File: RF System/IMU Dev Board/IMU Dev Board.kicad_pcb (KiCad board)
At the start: 2 copper layers, 27 x 26.5 mm, 12 parts, among them J1 Conn_01x08_Pin, J2 Conn_01x08_Pin, U1 BMI088

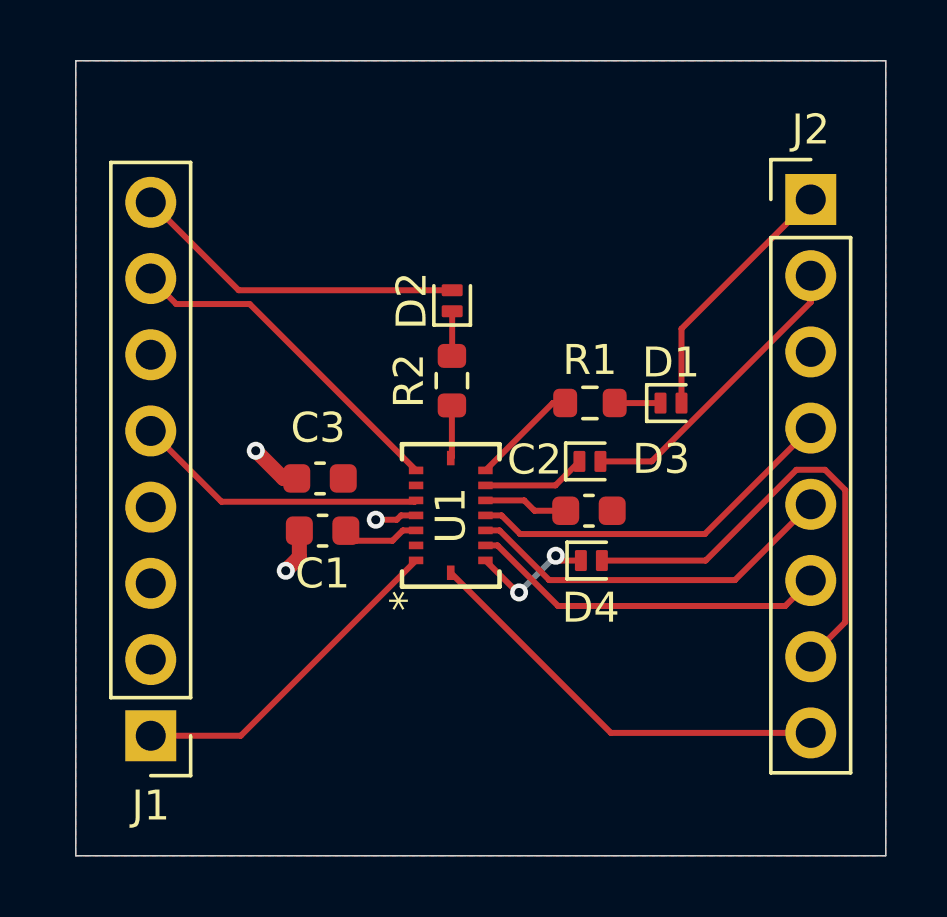
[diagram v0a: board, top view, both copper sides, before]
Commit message: IMU Dev Done
Finished IMU dev board and cleared all ERC and DRC. Design is controlled by the technical datasheet which required a strict symmetrical design within a few mm of each side of the IMU.
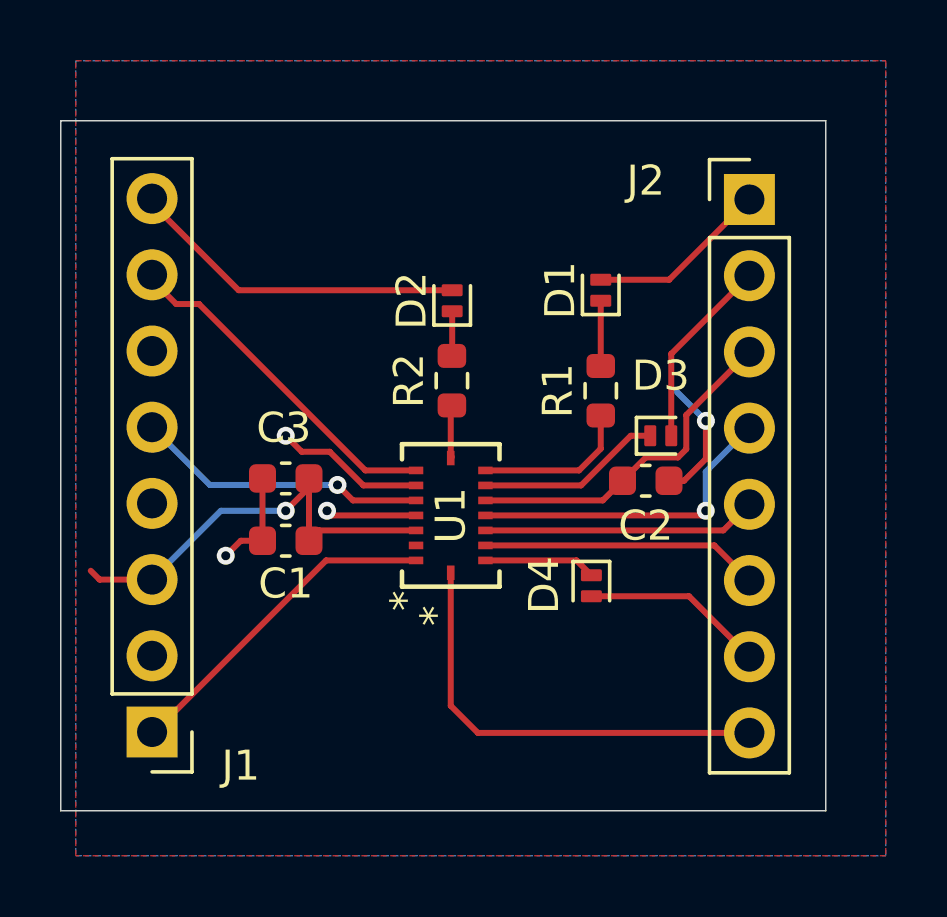
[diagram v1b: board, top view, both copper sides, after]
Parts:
- moved D1 4.43 mm to (174.5, 79.7), turned to 90 degrees
- moved D3 2.51 mm to (176.5, 84.5)
- moved C2 2.14 mm to (176.0, 86.0)
- moved J2 2.04 mm to (179.5, 76.6)
- moved C1 1.27 mm to (164.0, 88.0)
- moved C3 1.14 mm to (164.0, 85.9)
- moved D4 0.84 mm to (174.2, 89.5), turned to -90 degrees
- moved R1 0.54 mm to (174.5, 83.0), turned to 90 degrees
- moved J1 0.13 mm to (159.5, 94.4)
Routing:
- net +3.3V: track 5.44 -> 26.3 mm, vias 0 -> 1
- net GND: track 4.68 -> 15.8 mm, vias 3 -> 4
- net Net-(D4-A): track 15.7 -> 6.10 mm
- net Net-(D3-A): track 10.1 -> 6.41 mm
- net INT4: track 12.6 -> 9.16 mm
- net CSB1: track 12.0 -> 9.28 mm
- net SDO2: track 3.47 -> 6.18 mm
- net Net-(D1-A): track 8.57 -> 6.06 mm
- net INT3: track 12.6 -> 10.8 mm, vias 0 -> 1
- net Net-(U1-SDA/SDI): track 3.59 -> 5.25 mm
- net SDA/SDI: track 1.53 -> 2.17 mm
- net INT1: track 14.2 -> 14.8 mm
- net SDO1: track 4.20 -> 3.74 mm, vias 2 -> 0
- net CSB2: track 9.84 -> 9.81 mm, vias 0 -> 1
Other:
- board size 27 x 26.5 mm -> 25.5 x 23 mm

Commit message: RF + Telem (#9)
Co-authored-by: weijing-c <128620043+weijing-c@users.noreply.github.com>
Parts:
- C1, C2, C3: footprint Capacitor_SMD:C_0603_1608Metric -> Capacitor_SMD:C_0805_2012Metric
- R1, R2: footprint Resistor_SMD:R_0603_1608Metric -> Resistor_SMD:R_0805_2012Metric
- moved C1 1.12 mm to (163.0, 88.5)
- moved D3 1.00 mm to (176.5, 83.5)
- moved C3 0.77 mm to (163.3, 86.1)
- moved J1 0.54 mm to (159.0, 94.4)
- moved J2 0.54 mm to (180.0, 76.6)
- moved R1 0.50 mm to (174.5, 82.5)
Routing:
- net +3.3V: track 26.3 -> 36.0 mm, vias 1 -> 3
- net SDA/SDI: track 2.17 -> 0.00 mm
- net GND: track 15.8 -> 17.1 mm, vias 4 -> 3
- net Net-(D3-A): track 6.41 -> 5.41 mm
